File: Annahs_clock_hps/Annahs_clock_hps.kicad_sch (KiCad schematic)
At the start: 9 parts

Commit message: Slide 39
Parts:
- added C3, C4, C5, C6: 22pf, footprints:C_0805_2012Metric, symbol HPS:C_0805_22pf
- added D?: LED_0805, footprints:LED_0805_2012Metric, symbol HPS:LED_0805
- added J1: PJ-102AH, footprints:PJ-102AH, symbol HPS:PJ-102AH
- added J?: Conn_01x06, footprints:PinHeader_1x06_P2.54mm_Vertical, symbol HPS:Conn_01x06
- added R1: 2.2K, footprints:R_0805_2012Metric, symbol HPS:R_0805_2.2K
- added R2: 10K, footprints:R_0805_2012Metric, symbol HPS:R_0805_10K
- C7, C8: renamed from C?; value C_0805_22pf -> 22p
- Y1: renamed from Y?; value Crystal_16MHz -> Crystal 22p
- gave numbers to parts that had none: 2
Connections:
- net GND: now also C7.2, C8.2, UI.8 (GND), C3.2, C4.2, C5.2, D?.1 (K), J?.1 (Pin_1), J?.2 (Pin_2)
- net XTAL1: now reaches C7.1, UI.9 (XTAL1/PB6), Y1.1
- net XTAL2: now reaches C8.1, UI.10 (XTAL2/PB7), Y1.2
- net RESET: now reaches UI.1 (~{RESET}/PC6)
- net RESET: now also C6.2, R2.2
- net LED_SCK: now reaches UI.19 (PB5)
- net LED_SCK: now also R1.1
- net PD0: now reaches UI.2 (PD0)
- net PD0: now also J?.4 (Pin_4)
- net VCC: now reaches UI.20 (AVCC)
- net VCC: now also UI.7 (VCC), R2.1
- net PD1: now reaches UI.3 (PD1)
- net PD1: now also J?.5 (Pin_5)
- new net: D?.2 (A), R1.2
- new net RTS: C6.1, J?.6 (Pin_6)
- no-connect marks 0 -> 2
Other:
- moved on the sheet: C, C7, C8, UI, Y1

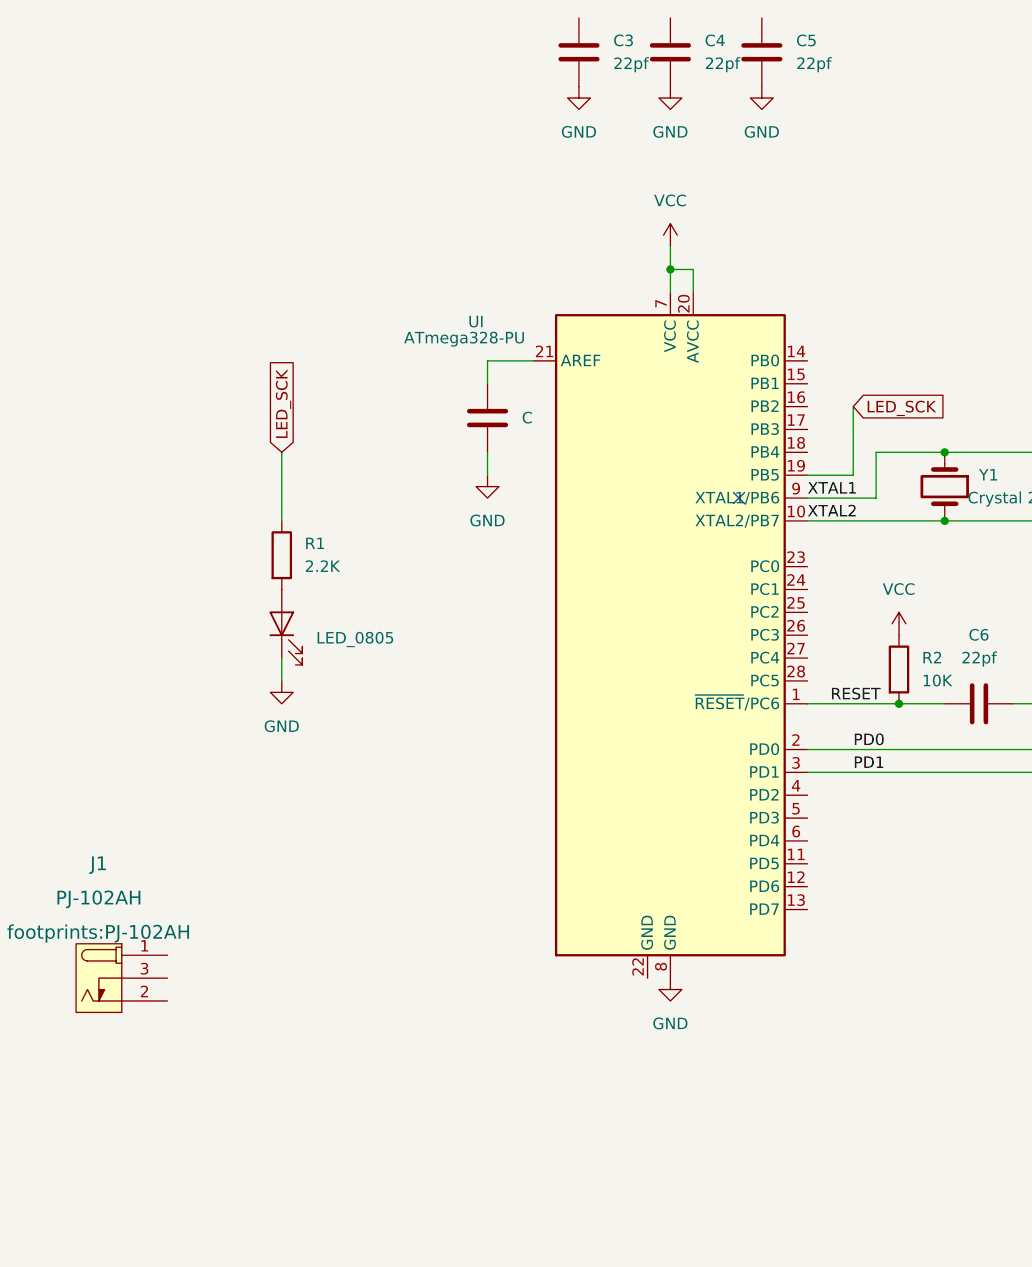
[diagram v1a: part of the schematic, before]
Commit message: Schematic Phase I
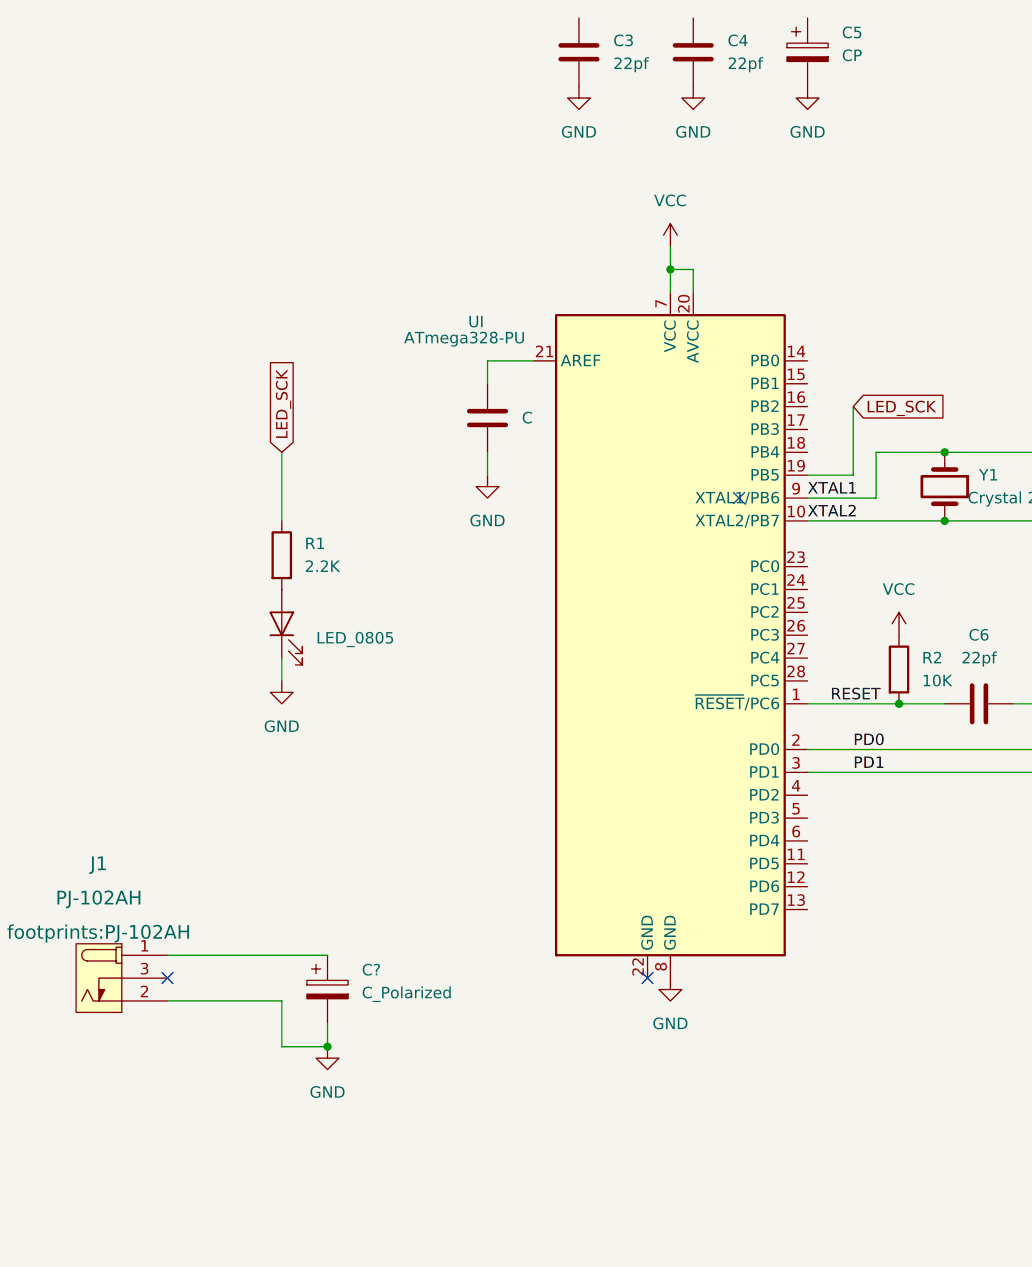
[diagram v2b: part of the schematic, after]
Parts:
- removed C5: 22pf, footprints:C_0805_2012Metric, symbol HPS:C_0805_22pf
- added C5: CP, symbol KICAD:C_Polarized
- added C?: C_Polarized, symbol KICAD:C_Polarized
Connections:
- net GND: now also J1.2 (OUT), C5.2, C?.2
- net at J1.1 (POLE): now also C?.1
- no-connect marks 2 -> 4
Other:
- moved on the sheet: C4

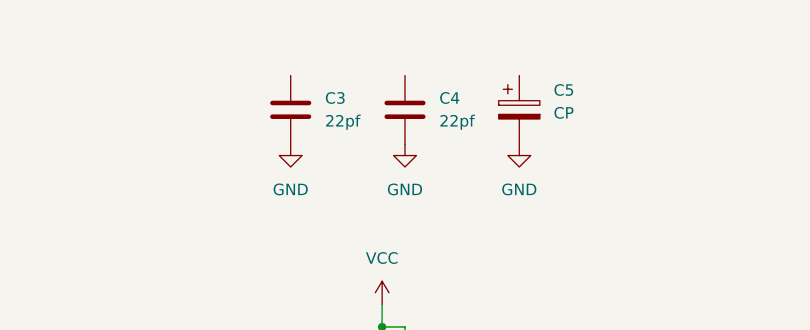
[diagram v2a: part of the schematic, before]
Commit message: Update Annahs_clock_hps.kicad_sch
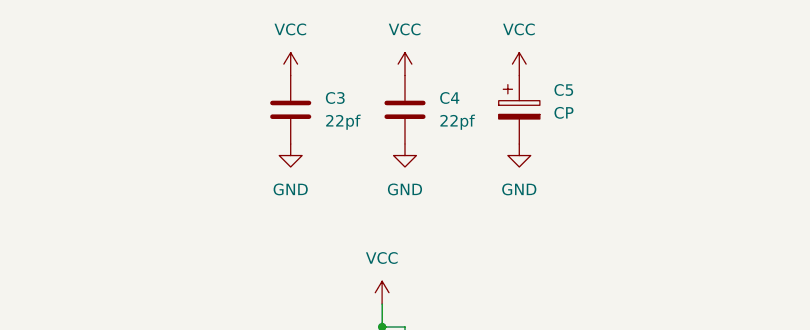
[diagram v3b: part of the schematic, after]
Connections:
- net VCC: now also C3.1, C4.1, C5.1
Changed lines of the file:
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@@
     )
+  )
+  (symbol (lib_id "HPS:VCC") (at 124.46 33.02 0) (unit 1)
+    (in_bom yes) (on_board yes) (fields_autoplaced)
+    (property "Reference" "#PWR?" (id 0) (at 124.46 36.83 0)
+      (effects (font (size 1.27 1.27)) hide)
+    )
+    (property "Value" "VCC" (id 1) (at 124.46 27.94 0))
+    (property "Footprint" "" (id 2) (at 124.46 33.02 0)
+      (effects (font (size 1.27 1.27)) hide)
+    )
+    (property "Datasheet" "" (id 3) (at 124.46 33.02 0)
+      (effects (font (size 1.27 1.27)) hide)
+    )
+    (pin "1")
   )
   (symbol (lib_id "HPS:MountingHole") (at 25.4 179.07 0) (unit 1)
@@
     (pin "2")
   )
+  (symbol (lib_id "HPS:VCC") (at 137.16 33.02 0) (unit 1)
+    (in_bom yes) (on_board yes) (fields_autoplaced)
+    (property "Reference" "#PWR?" (id 0) (at 137.16 36.83 0)
+      (effects (font (size 1.27 1.27)) hide)
+    )
+    (property "Value" "VCC" (id 1) (at 137.16 27.94 0))
+    (property "Footprint" "" (id 2) (at 137.16 33.02 0)
+      (effects (font (size 1.27 1.27)) hide)
+    )
+    (property "Datasheet" "" (id 3) (at 137.16 33.02 0)
+      (effects (font (size 1.27 1.27)) hide)
+    )
+    (pin "1")
+  )
   (symbol (lib_id "HPS:GND") (at 149.86 40.64 0) (unit 1)
     (in_bom yes) (on_board yes) (fields_autoplaced)
@@
     )
     (property "Datasheet" "" (id 3) (at 96.52 147.32 0)
+      (effects (font (size 1.27 1.27)) hide)
+    )
+    (pin "1")
+  )
+  (symbol (lib_id "HPS:VCC") (at 149.86 33.02 0) (unit 1)
+    (in_bom yes) (on_board yes) (fields_autoplaced)
+    (property "Reference" "#PWR?" (id 0) (at 149.86 36.83 0)
+      (effects (font (size 1.27 1.27)) hide)
+    )
+    (property "Value" "VCC" (id 1) (at 149.86 27.94 0))
+    (property "Footprint" "" (id 2) (at 149.86 33.02 0)
+      (effects (font (size 1.27 1.27)) hide)
+    )
+    (property "Datasheet" "" (id 3) (at 149.86 33.02 0)
       (effects (font (size 1.27 1.27)) hide)
     )
@@
       (reference "#PWR?") (unit 1) (value "GND") (footprint "")
     )
+    (path "/2e84fd9d-f40c-4116-8b8f-5bdeef4ab66f"
+      (reference "#PWR?") (unit 1) (value "VCC") (footprint "")
+    )
     (path "/5f945b73-5855-4b4e-95a7-c5d92ec1256c"
       (reference "#PWR?") (unit 1) (value "VCC") (footprint "")
     )
+    (path "/743bfacd-802c-4d0b-bb24-4fad5a501214"
+      (reference "#PWR?") (unit 1) (value "VCC") (footprint "")
+    )
     (path "/7f76fa8c-ef00-48fc-a127-184b217b1c7c"
       (reference "#PWR?") (unit 1) (value "GND") (footprint "")
@@
       (reference "#PWR?") (unit 1) (value "GND") (footprint "")
     )
+    (path "/85527b9e-fc32-4d5e-9c6e-d7b75d39cdfe"
+      (reference "#PWR?") (unit 1) (value "VCC") (footprint "")
+    )
     (path "/8fb60f21-2946-4698-ab02-c271abf87f0e"

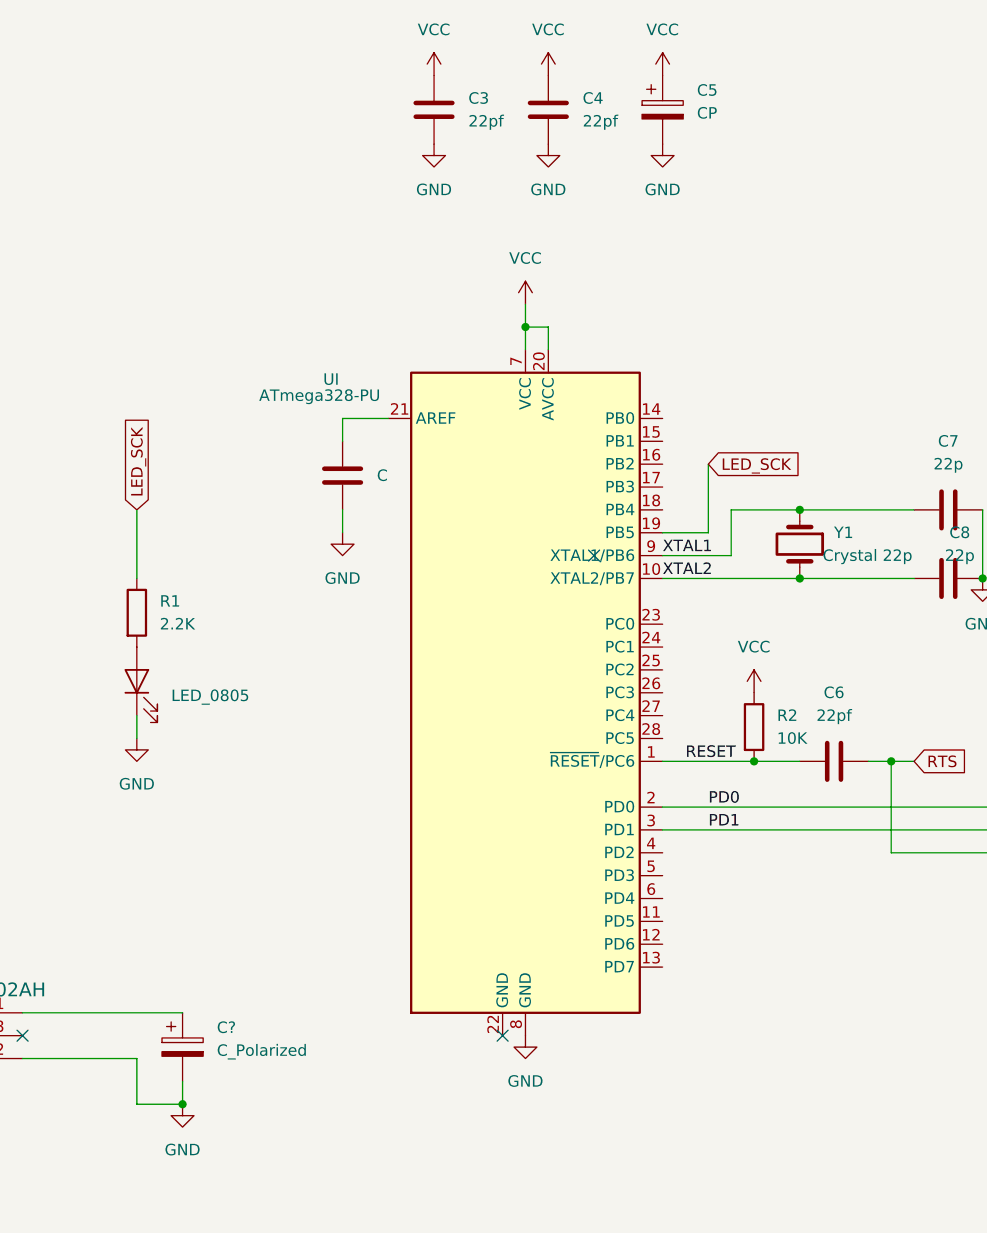
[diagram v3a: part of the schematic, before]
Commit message: Schematic Phase I
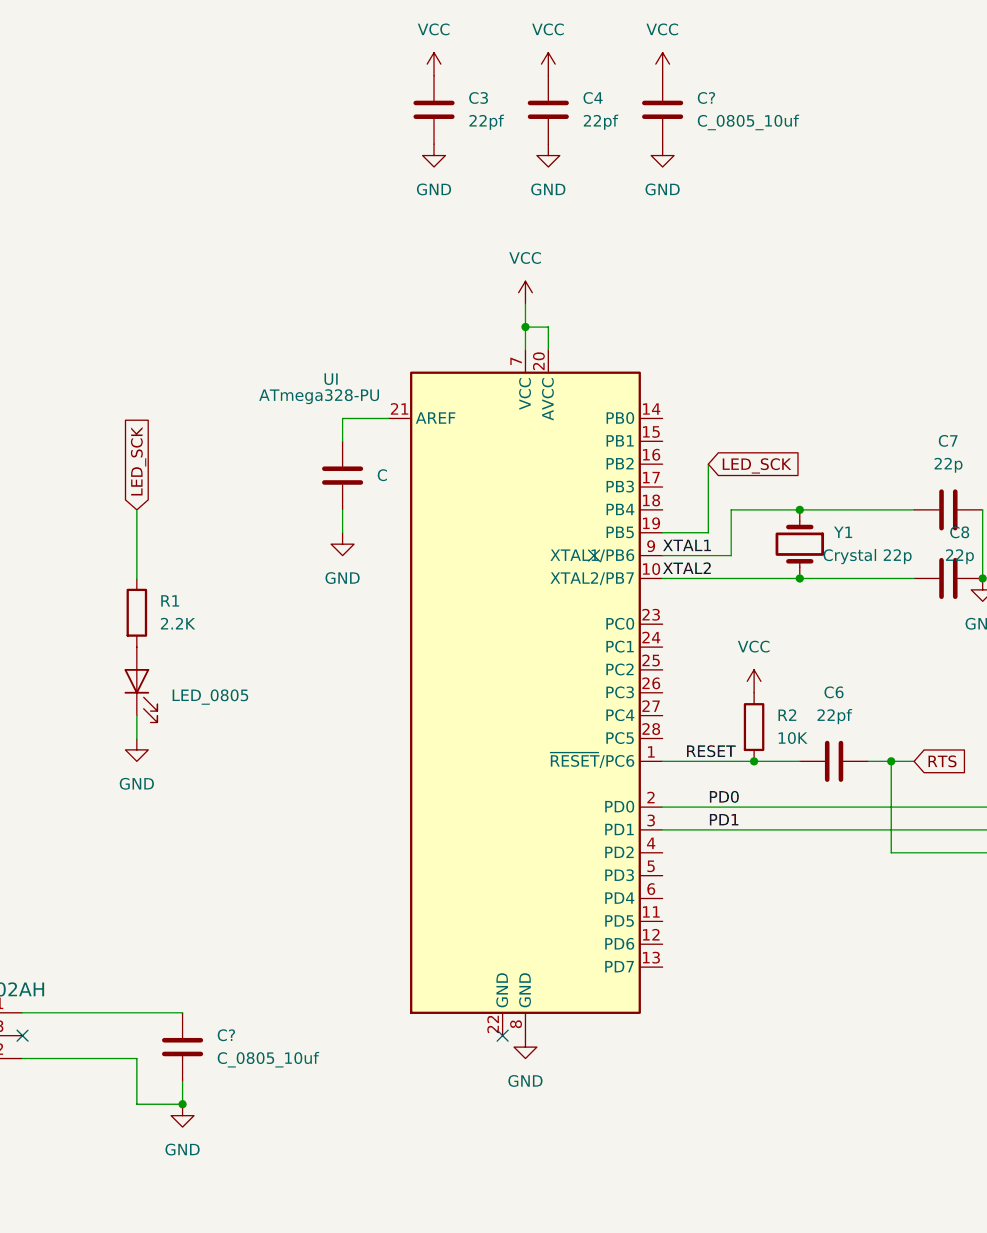
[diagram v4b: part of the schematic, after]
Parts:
- removed C5: CP, symbol KICAD:C_Polarized
- removed C?: C_Polarized, symbol KICAD:C_Polarized
- added C? (x2): C_0805_10uf, footprints:C_0805_2012Metric, symbol HPS:C_0805_10uf
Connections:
- net GND: now also C?.2, C?.2
- net VCC: now also C?.1
- net at J1.1 (POLE): now also C?.1
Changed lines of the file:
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@@
     )
+  )
+  (symbol (lib_id "HPS:C_0805_10uf") (at 149.86 36.83 0) (unit 1)
+    (in_bom yes) (on_board yes) (fields_autoplaced)
+    (property "Reference" "C?" (id 0) (at 153.67 35.5599 0)
+      (effects (font (size 1.27 1.27)) (justify left))
+    )
+    (property "Value" "C_0805_10uf" (id 1) (at 153.67 38.0999 0)
+      (effects (font (size 1.27 1.27)) (justify left))
+    )
+    (property "Footprint" "footprints:C_0805_2012Metric" (id 2) (at 150.8252 40.64 0)
+      (effects (font (size 1.27 1.27)) hide)
+    )
+    (property "Datasheet" "https://search.murata.co.jp/Ceramy/image/img/A01X/G101/ENG/GRM21BR61E106KA73-01.pdf" (id 3) (at 150.495 34.29 0)
+      (effects (font (size 1.27 1.27)) hide)
+    )
+    (property "MFG" "Murata Electronics" (id 4) (at 149.86 43.18 0)
+      (effects (font (size 1.27 1.27)) hide)
+    )
+    (property "MPN" "GRM21BR61E106KA73L" (id 5) (at 149.86 45.72 0)
+      (effects (font (size 1.27 1.27)) hide)
+    )
+    (property "Digikey PN" "490-5523-1-ND" (id 6) (at 149.86 50.8 0)
+      (effects (font (size 1.27 1.27)) hide)
+    )
+    (property "Mouser PN" "N/A" (id 7) (at 149.86 53.34 0)
+      (effects (font (size 1.27 1.27)) hide)
+    )
+    (property "Voltage" "N/A" (id 8) (at 149.86 55.88 0)
+      (effects (font (size 1.27 1.27)) hide)
+    )
+    (property "Dielectric" "N/A" (id 9) (at 149.86 55.88 0)
+      (effects (font (size 1.27 1.27)) hide)
+    )
+    (property "Tolerance" "N/A" (id 10) (at 149.86 55.88 0)
+      (effects (font (size 1.27 1.27)) hide)
+    )
+    (pin "1")
+    (pin "2")
   )
   (symbol (lib_id "HPS:GND") (at 134.62 139.7 0) (unit 1)
@@
     (pin "2")
   )
-  (symbol (lib_id "KICAD:C_Polarized") (at 96.52 140.97 0) (unit 1)
-    (in_bom yes) (on_board yes) (fields_autoplaced)
-    (property "Reference" "C?" (id 0) (at 100.33 138.8109 0)
-      (effects (font (size 1.27 1.27)) (justify left))
-    )
-    (property "Value" "C_Polarized" (id 1) (at 100.33 141.3509 0)
-      (effects (font (size 1.27 1.27)) (justify left))
-    )
-    (property "Footprint" "" (id 2) (at 97.4852 144.78 0)
-      (effects (font (size 1.27 1.27)) hide)
-    )
-    (property "Datasheet" "~" (id 3) (at 96.52 140.97 0)
-      (effects (font (size 1.27 1.27)) hide)
-    )
-    (pin "1")
-    (pin "2")
-  )
   (symbol (lib_id "HPS:PJ-102AH") (at 73.66 139.7 0) (unit 1)
     (in_bom yes) (on_board yes) (fields_autoplaced)
@@
     (pin "2")
     (pin "3")
-  )
-  (symbol (lib_id "KICAD:C_Polarized") (at 149.86 36.83 0) (unit 1)
-    (in_bom yes) (on_board yes)
-    (property "Reference" "C5" (id 0) (at 153.67 34.6709 0)
-      (effects (font (size 1.27 1.27)) (justify left))
-    )
-    (property "Value" "CP" (id 1) (at 153.67 37.2109 0)
-      (effects (font (size 1.27 1.27)) (justify left))
-    )
-    (property "Footprint" "" (id 2) (at 150.8252 40.64 0)
-      (effects (font (size 1.27 1.27)) hide)
-    )
-    (property "Datasheet" "~" (id 3) (at 149.86 36.83 0)
-      (effects (font (size 1.27 1.27)) hide)
-    )
-    (pin "1")
-    (pin "2")
   )
   (symbol (lib_id "HPS:MountingHole") (at 45.72 179.07 0) (unit 1)
@@
     (pin "2")
   )
+  (symbol (lib_id "HPS:C_0805_10uf") (at 96.52 140.97 0) (unit 1)
+    (in_bom yes) (on_board yes) (fields_autoplaced)
+    (property "Reference" "C?" (id 0) (at 100.33 139.6999 0)
+      (effects (font (size 1.27 1.27)) (justify left))
+    )
+    (property "Value" "C_0805_10uf" (id 1) (at 100.33 142.2399 0)
+      (effects (font (size 1.27 1.27)) (justify left))
+    )
+    (property "Footprint" "footprints:C_0805_2012Metric" (id 2) (at 97.4852 144.78 0)
+      (effects (font (size 1.27 1.27)) hide)
+    )
+    (property "Datasheet" "https://search.murata.co.jp/Ceramy/image/img/A01X/G101/ENG/GRM21BR61E106KA73-01.pdf" (id 3) (at 97.155 138.43 0)
+      (effects (font (size 1.27 1.27)) hide)
+    )
+    (property "MFG" "Murata Electronics" (id 4) (at 96.52 147.32 0)
+      (effects (font (size 1.27 1.27)) hide)
+    )
+    (property "MPN" "GRM21BR61E106KA73L" (id 5) (at 96.52 149.86 0)
+      (effects (font (size 1.27 1.27)) hide)
+    )
+    (property "Digikey PN" "490-5523-1-ND" (id 6) (at 96.52 154.94 0)
+      (effects (font (size 1.27 1.27)) hide)
+    )
+    (property "Mouser PN" "N/A" (id 7) (at 96.52 157.48 0)
+      (effects (font (size 1.27 1.27)) hide)
+    )
+    (property "Voltage" "N/A" (id 8) (at 96.52 160.02 0)
+      (effects (font (size 1.27 1.27)) hide)
+    )
+    (property "Dielectric" "N/A" (id 9) (at 96.52 160.02 0)
+      (effects (font (size 1.27 1.27)) hide)
+    )
+    (property "Tolerance" "N/A" (id 10) (at 96.52 160.02 0)
+      (effects (font (size 1.27 1.27)) hide)
+    )
+    (pin "1")
+    (pin "2")
+  )
   (symbol (lib_id "HPS:VCC") (at 160.02 101.6 0) (unit 1)
     (in_bom yes) (on_board yes) (fields_autoplaced)
@@
       (reference "C4") (unit 1) (value "22pf") (footprint "footprints:C_0805_2012Metric")
     )
-    (path "/2696cfef-2893-427e-8025-c3f76e6e7889"
-      (reference "C5") (unit 1) (value "CP") (footprint "")
-    )
     (path "/71aa514f-edec-4b48-b4fc-619d89434bf1"
       (reference "C6") (unit 1) (value "22pf") (footprint "footprints:C_0805_2012Metric")
@@
       (reference "C8") (unit 1) (value "22p") (footprint "footprints:C_0805_2012Metric")
     )
-    (path "/14021e5c-d6e4-40c9-8839-bb66e7b3c55c"
-      (reference "C?") (unit 1) (value "C_Polarized") (footprint "")
+    (path "/034bd053-1ff2-40c8-8b16-3f5f12183565"
+      (reference "C?") (unit 1) (value "C_0805_10uf") (footprint "footprints:C_0805_2012Metric")
+    )
+    (path "/efc9483b-a294-4565-871b-a13e684c7423"
+      (reference "C?") (unit 1) (value "C_0805_10uf") (footprint "footprints:C_0805_2012Metric")
     )
     (path "/eae694eb-ba06-4cce-ba6f-82045a997170"
